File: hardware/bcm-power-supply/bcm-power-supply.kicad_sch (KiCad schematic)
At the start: 24 parts, among them J1 Screw_Terminal_01x02, J2 Conn_02x08_Odd_Even, J3 Conn_02x08_Odd_Even, J4 Conn_01x04, J5 Conn_01x04, U1 N7812, U2 N7812

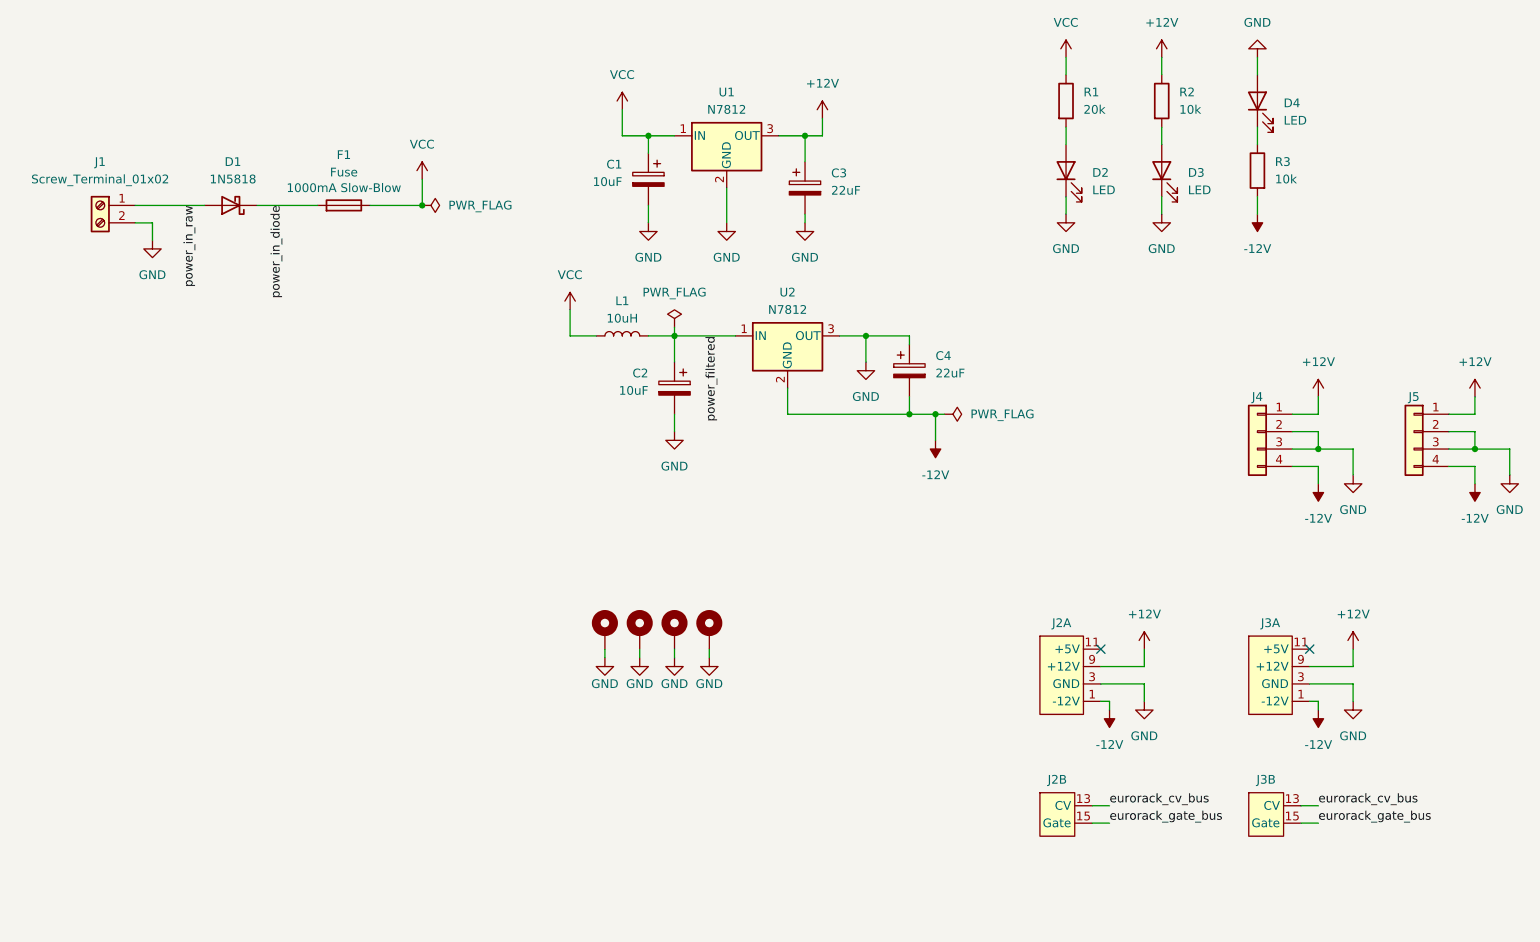
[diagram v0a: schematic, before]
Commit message: Updating with 5v output
And making the board smaller
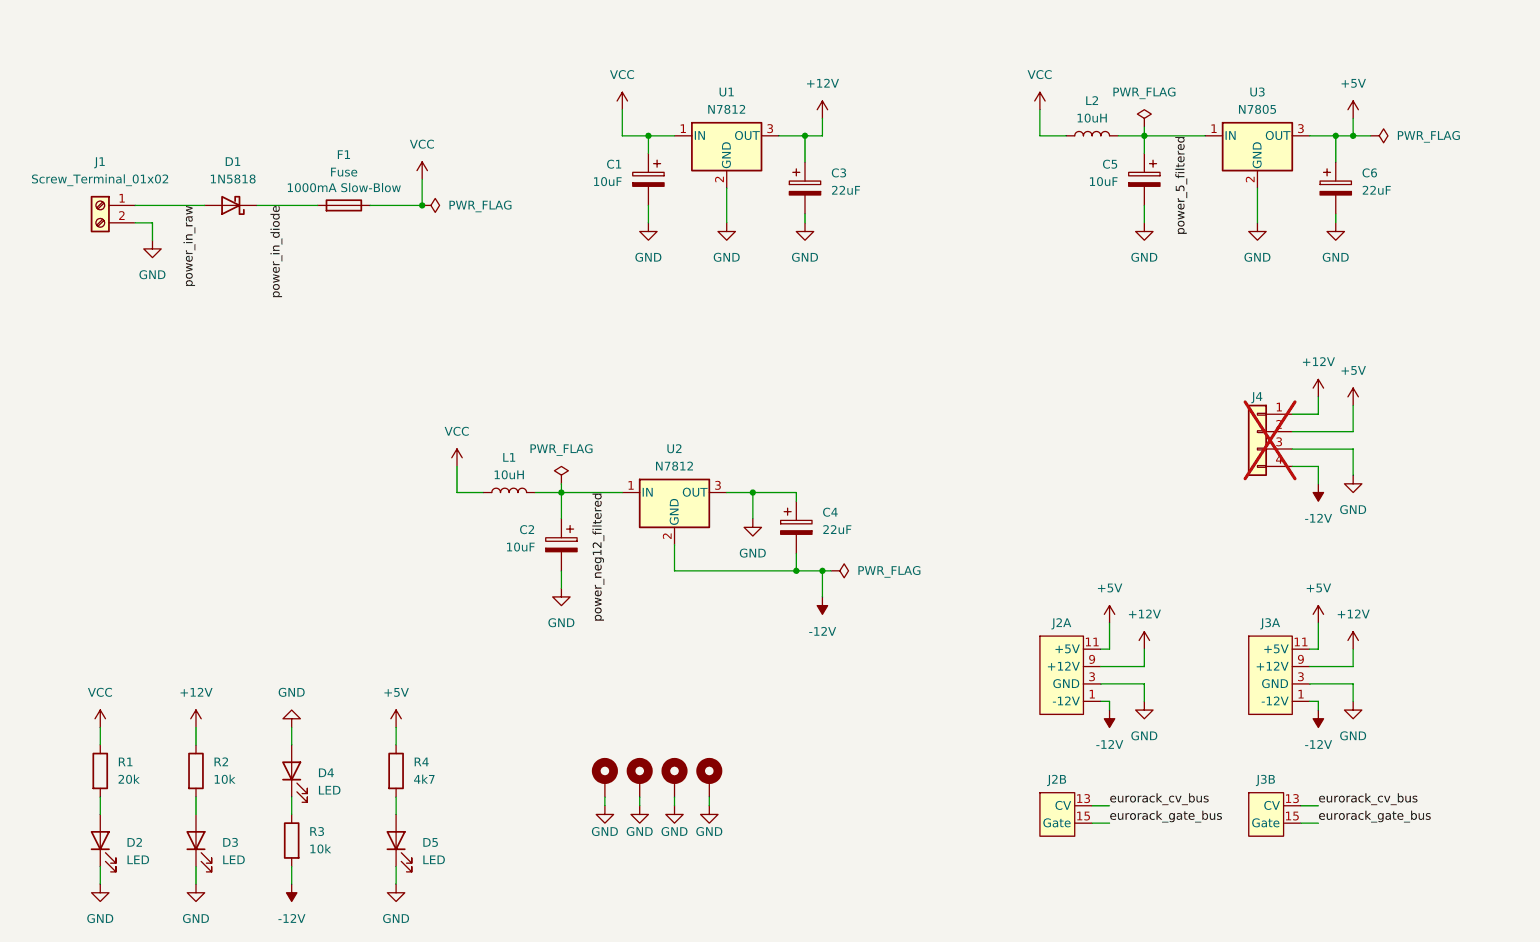
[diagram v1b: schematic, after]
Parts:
- removed J5: Conn_01x04, Connector_Molex:Molex_KK-396_A-41792-0004_1x04_P3.96mm_Horizontal, symbol Connector_Generic:Conn_01x04
- added C5: 10uF, Capacitor_THT:CP_Radial_D6.3mm_P2.50mm, symbol Device:C_Polarized
- added C6: 22uF, Capacitor_THT:CP_Radial_D6.3mm_P2.50mm, symbol Device:C_Polarized
- added D5: LED, LED_THT:LED_D3.0mm, symbol Device:LED
- added L2: 10uH, Inductor_THT:L_Toroid_Vertical_L10.0mm_W5.0mm_P5.08mm, symbol Device:L
- added R4: 4k7, Resistor_THT:R_Axial_DIN0207_L6.3mm_D2.5mm_P10.16mm_Horizontal, symbol Device:R
- added U3: N7805, Package_TO_SOT_THT:TO-220-3_Horizontal_TabDown, symbol bcm-power-parts:N7805
- D2, D3, D4: footprint LED_THT:LED_D5.0mm -> LED_THT:LED_D3.0mm
- F1: MPR 05200101Z -> 05200001N
- J4: now not fitted
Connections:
- net GND: now also C5.2, C6.2, D5.1 (K), U3.2 (GND); no longer J4.2 (Pin_2)
- net VCC: now also L2.1
- net +5V: now reaches J2.11 (+5V), J2.12 (+5V)
- net +5V: now also J3.11 (+5V), J3.12 (+5V), J4.2 (Pin_2), C6.1, R4.1, U3.3 (OUT)
- net power_filtered renamed power_neg12_filtered
- new net: D5.2 (A), R4.2
- new net power_5_filtered: C5.1, L2.2, U3.1 (IN)
- no-connect marks 2 -> 0
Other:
- moved on the sheet: C2, C4, D2, D3, D4, L1, R1, R2, R3, U2

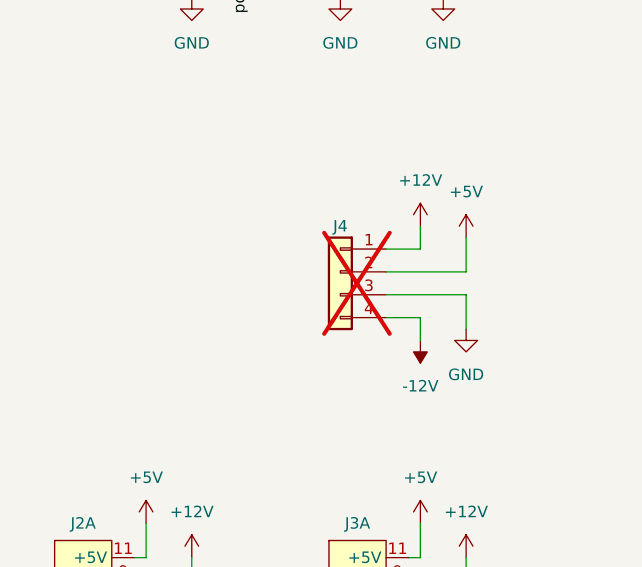
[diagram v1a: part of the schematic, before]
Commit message: Updating power supply board to give more space for regulators
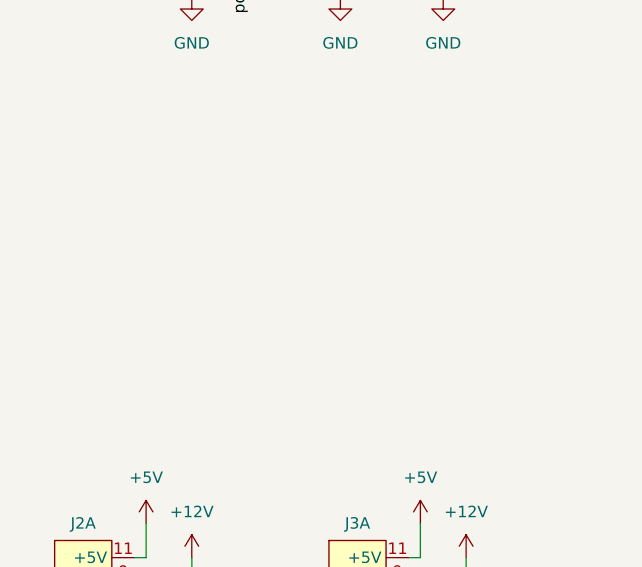
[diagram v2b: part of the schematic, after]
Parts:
- removed J4: Conn_01x04, Connector_Molex:Molex_KK-396_A-41792-0004_1x04_P3.96mm_Horizontal, symbol Connector_Generic:Conn_01x04
